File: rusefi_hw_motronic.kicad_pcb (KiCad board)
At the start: 2 copper layers, 175 x 129 mm, 45 parts, among them J1 OMEGA PCC_SMP_K, J2 Conn_01x02_Female, Q1 ZXTN2040, U1 SFH617A-2X009T, U2 BOSCH_55P, U3 molex_48pin_MRE, U4 MAX31855KASA, U5 TPIC8101, U6 MPXA4250A6U, U7 TE_6437288-6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

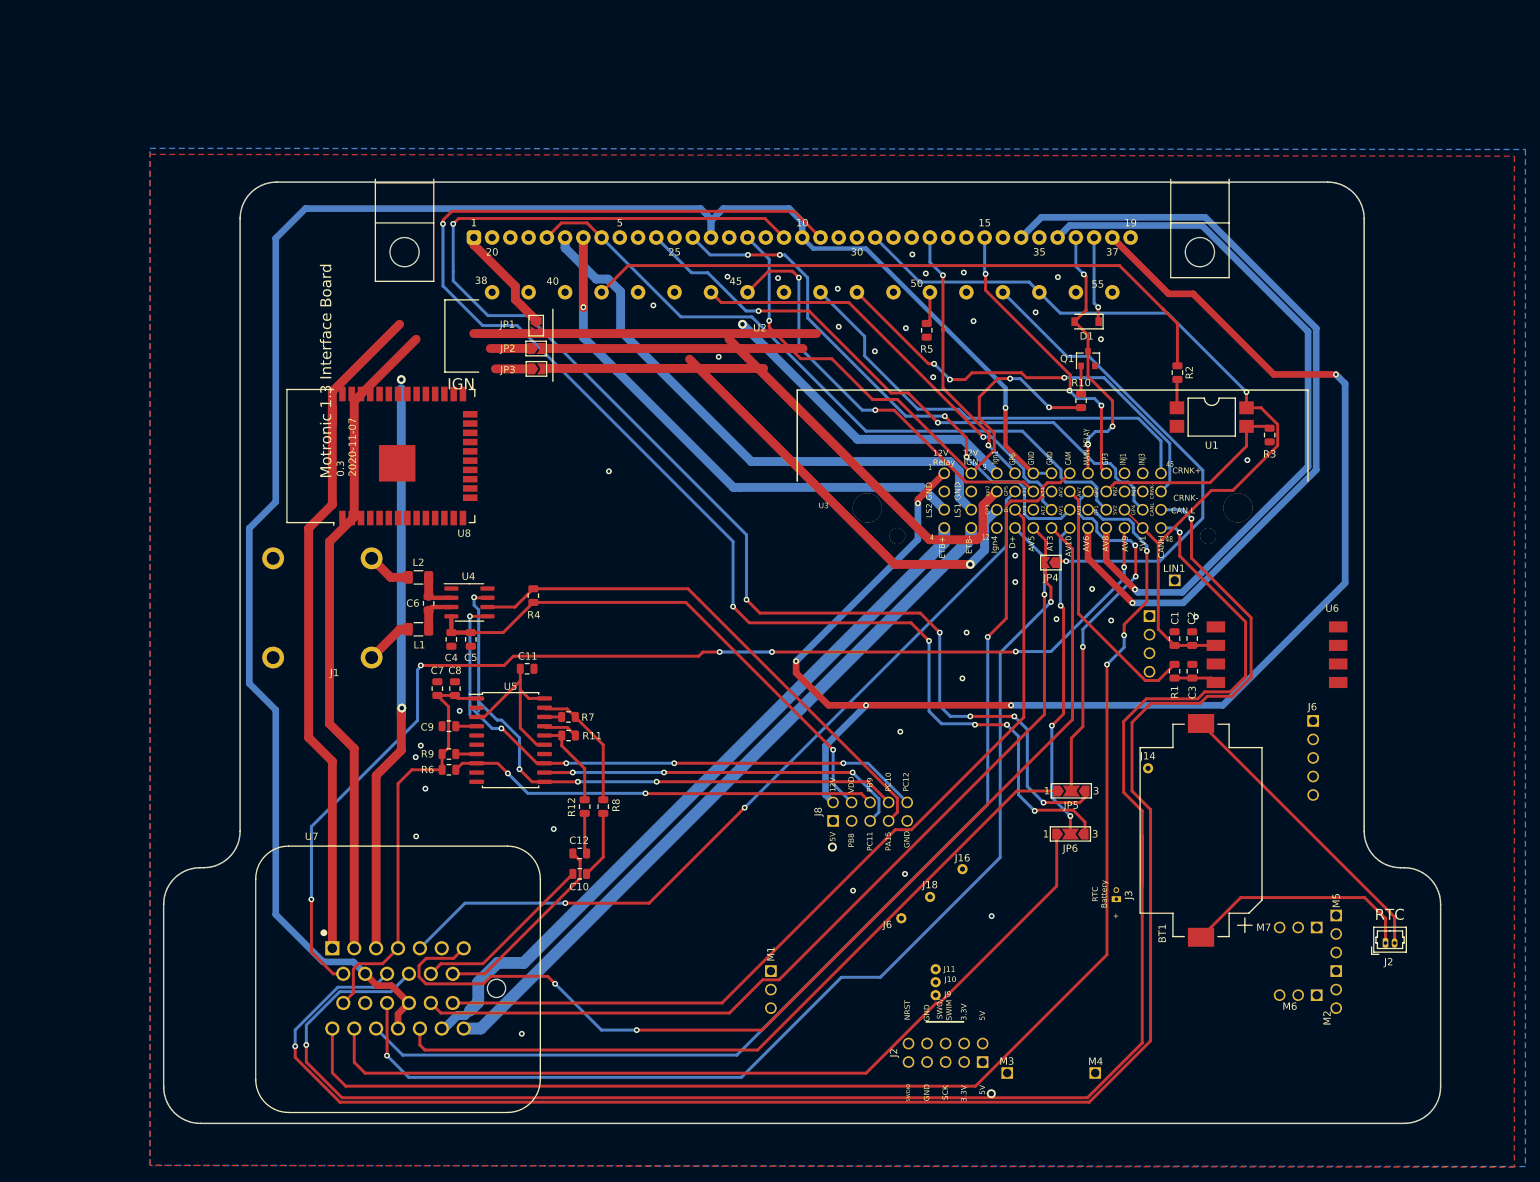
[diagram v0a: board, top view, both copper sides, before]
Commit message: updated layout for esp32
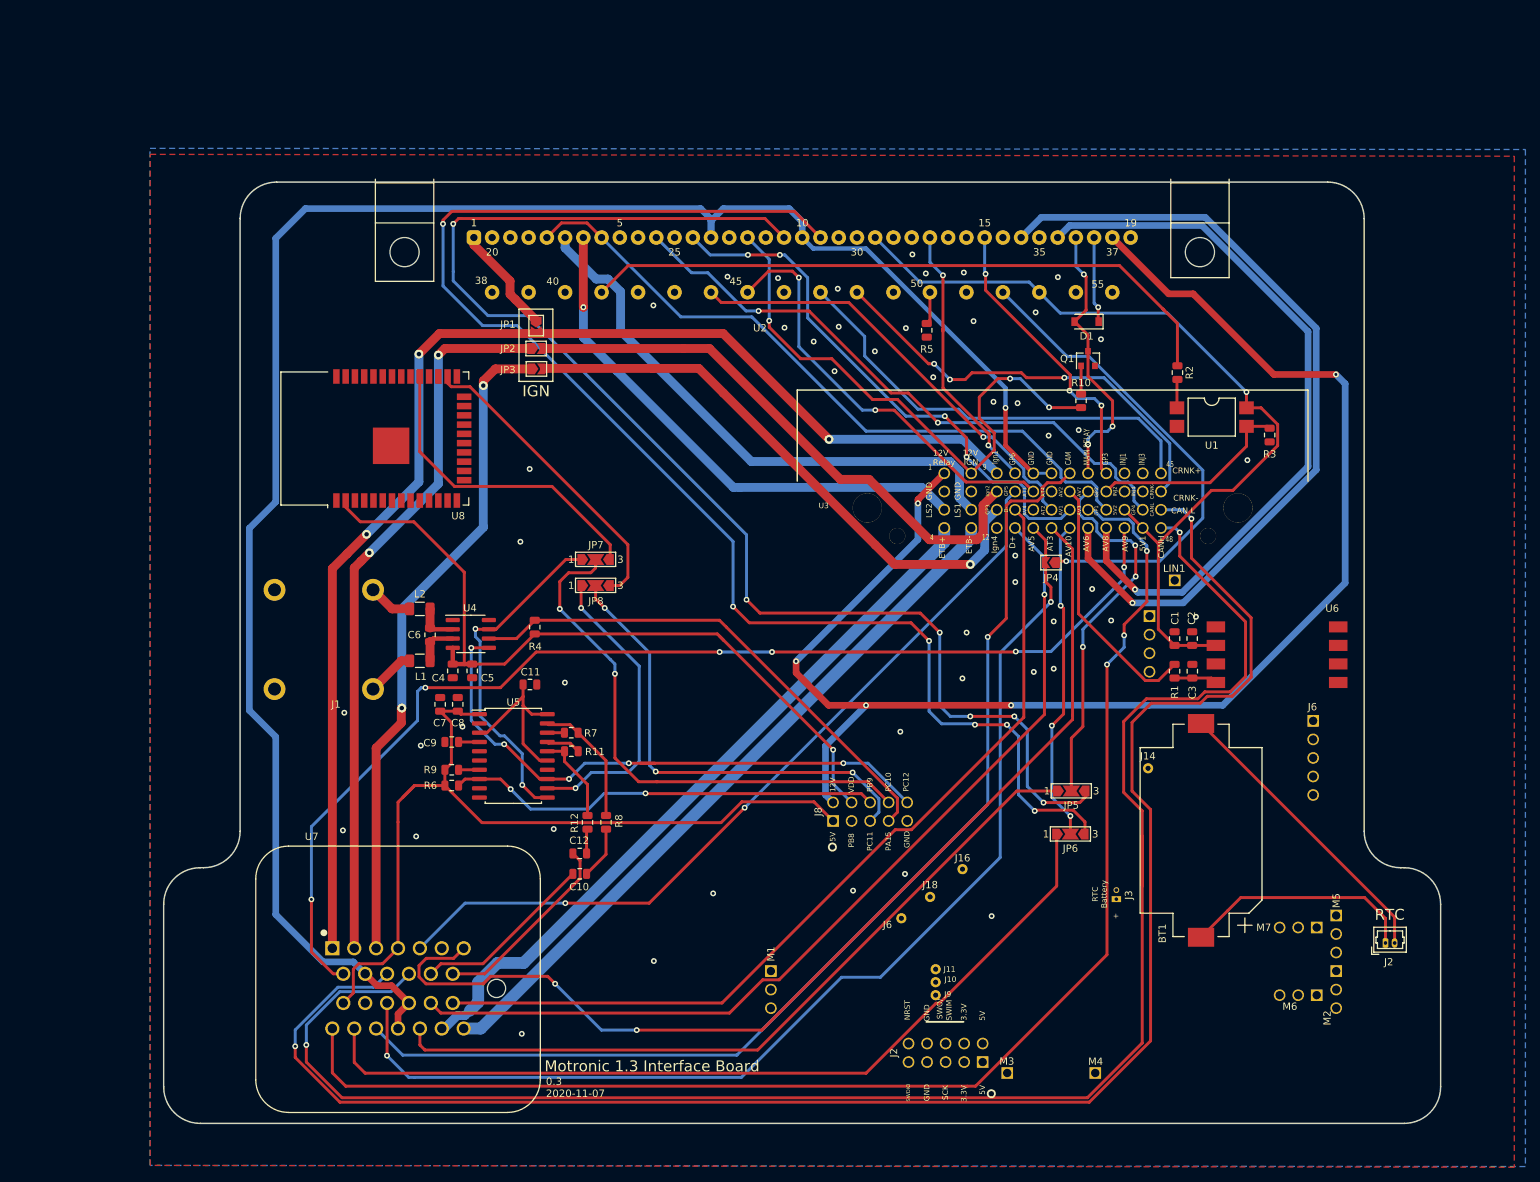
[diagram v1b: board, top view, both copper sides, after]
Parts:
- added JP7: SolderJumper_3_Open, Jumper:SolderJumper-3_P2.0mm_Open_TrianglePad1.0x1.5mm_NumberLabels, F.Cu at (82.4, 79.5)
- added JP8: SolderJumper_3_Open, Jumper:SolderJumper-3_P2.0mm_Open_TrianglePad1.0x1.5mm_NumberLabels, F.Cu at (82.4, 83.0)
- moved R4 4.32 mm to (74.0, 88.7)
- moved U4 4.32 mm to (65.3, 89.7)
- moved C4 4.32 mm to (62.8, 94.7)
- moved C5 4.32 mm to (65.5, 94.7)
- moved C6 4.32 mm to (59.7, 89.8)
- moved J1 4.32 mm to (51.9, 90.4)
- moved L1 4.32 mm to (58.3, 93.3)
- moved L2 4.32 mm to (58.3, 86.2)
- moved U8 2.54 mm to (55.1, 62.9)
- moved C7 2.19 mm to (61.1, 99.3)
- moved C8 2.19 mm to (63.5, 99.3)
- moved C9 2.19 mm to (62.7, 104.5)
- moved R11 2.19 mm to (79.1, 105.7)
- moved R12 2.19 mm to (81.3, 115.5)
- moved R6 2.19 mm to (62.7, 110.4)
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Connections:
- U3 pad J805: MOSI -> PC11
- U3 pad J808: MISO -> PC10
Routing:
- net PC10: track 0.00 -> 74.2 mm, vias 0 -> 2
- net PC11: track 0.00 -> 64.6 mm, vias 0 -> 3
- net +5V: track 177.6 -> 235.5 mm
- net TS_WIFI_TX: track 0.00 -> 43.7 mm
- net TS_WIFI_RX: track 0.00 -> 42.2 mm
- net MISO: track 82.1 -> 47.0 mm, vias 4 -> 2
- net +3V3: track 72.9 -> 105.2 mm
- net IGN_C: track 89.3 -> 78.6 mm
- net IGN_B: track 88.6 -> 77.9 mm
- net IGN1: track 185.2 -> 174.6 mm, vias 1 -> 3
- net MOSI: track 50.9 -> 41.5 mm, vias 3 -> 2
- net IGN3: track 84.3 -> 91.1 mm
- net IGN2: track 95.3 -> 99.1 mm, vias 0 -> 2
- net Net-(C10-Pad1): track 9.23 -> 7.23 mm
- net CS_EGT: track 72.7 -> 70.7 mm
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
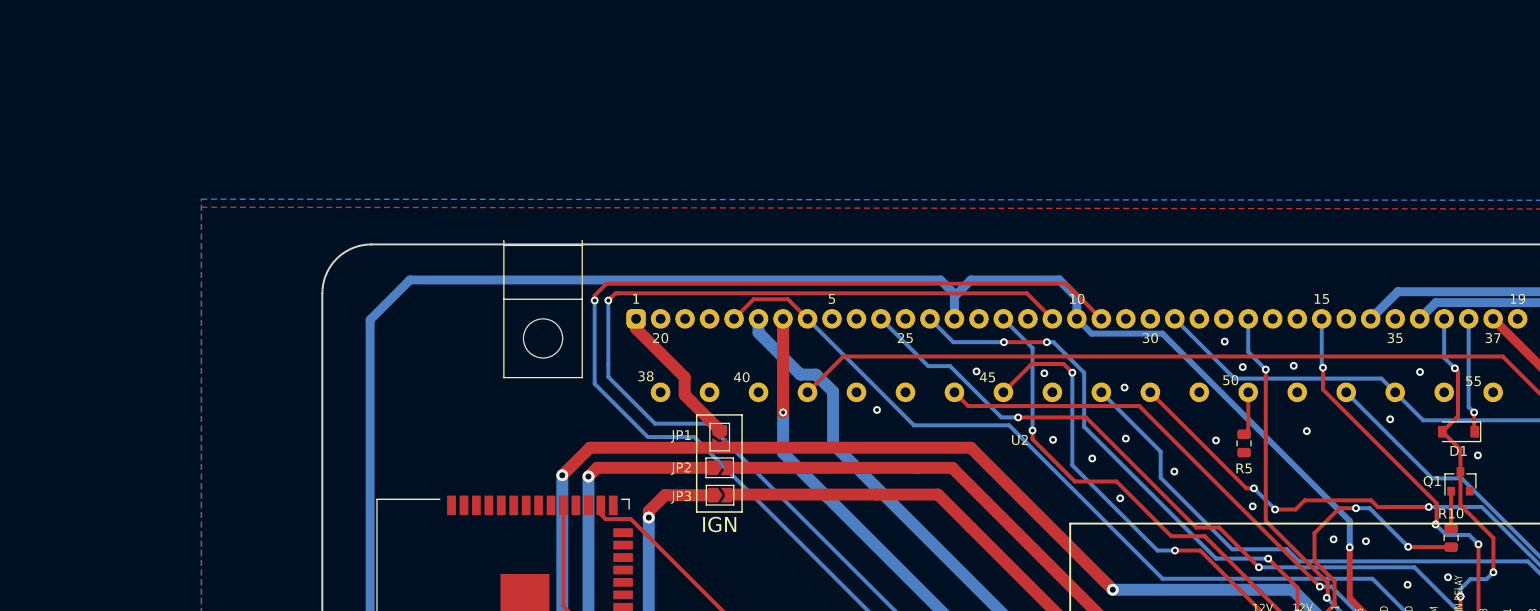
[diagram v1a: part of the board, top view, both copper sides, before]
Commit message: added igbts
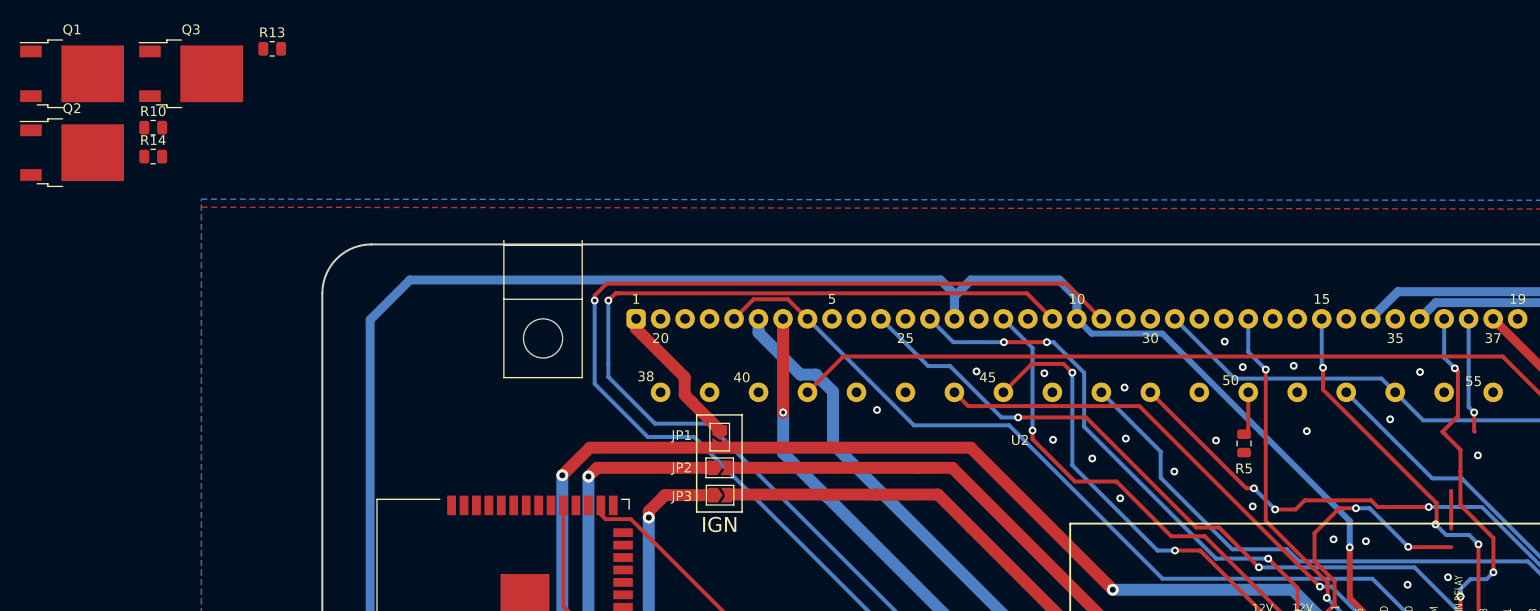
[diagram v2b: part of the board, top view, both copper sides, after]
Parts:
- removed D1: D, Diode_SMD:D_SOD-123
- added Q2: Q_NIGBT_CEG, Package_TO_SOT_SMD:TO-252-2, F.Cu at (8.12, 18.4)
- added Q3: Q_NIGBT_CEG, Package_TO_SOT_SMD:TO-252-2, F.Cu at (20.3, 10.3)
- added R13: 220, Resistor_SMD:R_0805_2012Metric, F.Cu at (28.5, 7.77)
- added R14: 220, Resistor_SMD:R_0805_2012Metric, F.Cu at (16.4, 18.8)
- Q1: value ZXTN2040 -> Q_NIGBT_CEG; footprint Package_TO_SOT_SMD:SOT-23 -> Package_TO_SOT_SMD:TO-252-2
- R10: value 7.5K -> 220
- moved Q1 147.7 mm to (8.12, 10.3), turned to 0 degrees
- moved R10 139.0 mm to (16.4, 15.8), turned to 0 degrees
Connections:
- JP2 pad 1: IGN2 -> Net-(JP2-Pad1)
- JP2 pad 2: IGN_B -> Net-(JP2-Pad2)
- JP3 pad 1: IGN3 -> Net-(JP3-Pad1)
- JP3 pad 2: IGN_C -> Net-(JP3-Pad2)
- Q1 pad 1: Net-(Q1-Pad1) -> Net-(JP3-Pad2)
- Q1 pad 2: GND -> IGN3
- Q1 pad 3: ECM_RELAY -> GND
- R10 pad 1: IGN_SWITCH -> IGN_C
- R10 pad 2: Net-(Q1-Pad1) -> Net-(JP3-Pad1)
- U3 pad 9: IGN1 -> IGN_A
